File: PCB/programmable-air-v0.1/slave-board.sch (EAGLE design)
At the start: 18 parts, among them Q1 600mA/40V, Q2 600mA/40V, Q3 600mA/40V

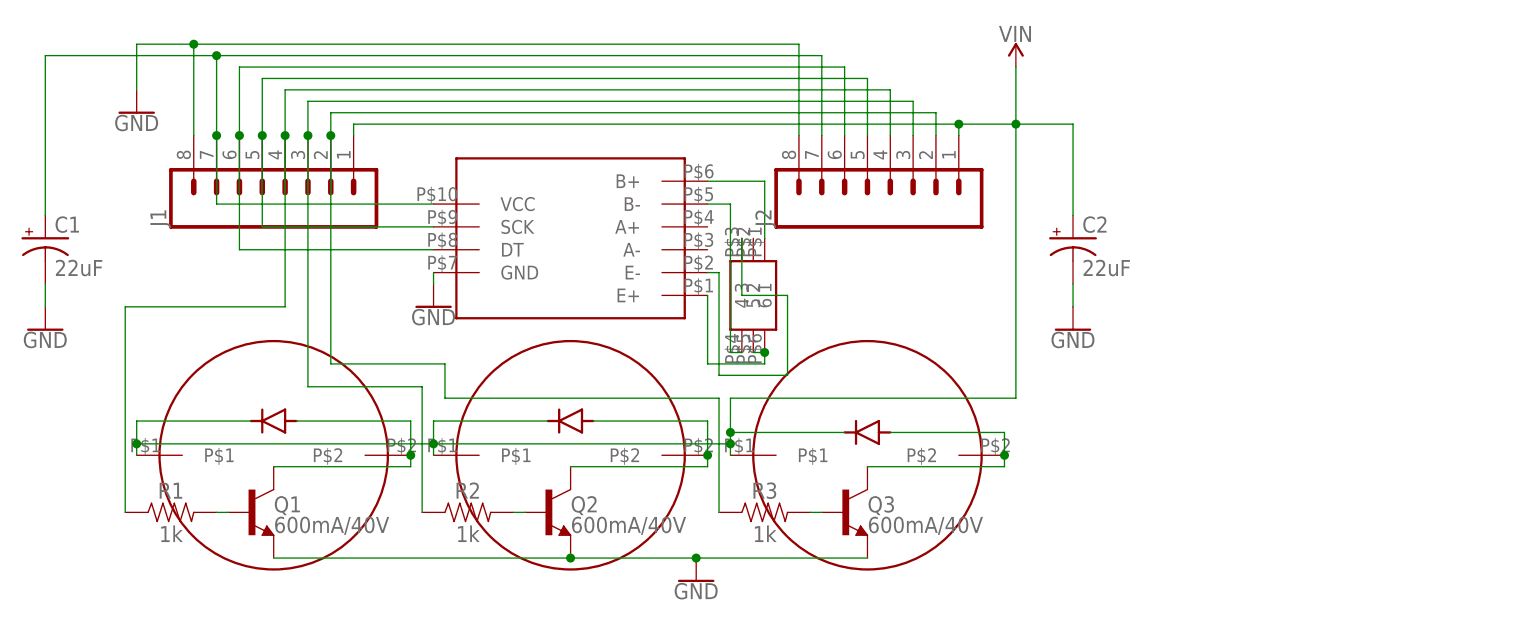
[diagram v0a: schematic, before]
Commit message: Modified slave board to have LM10CN
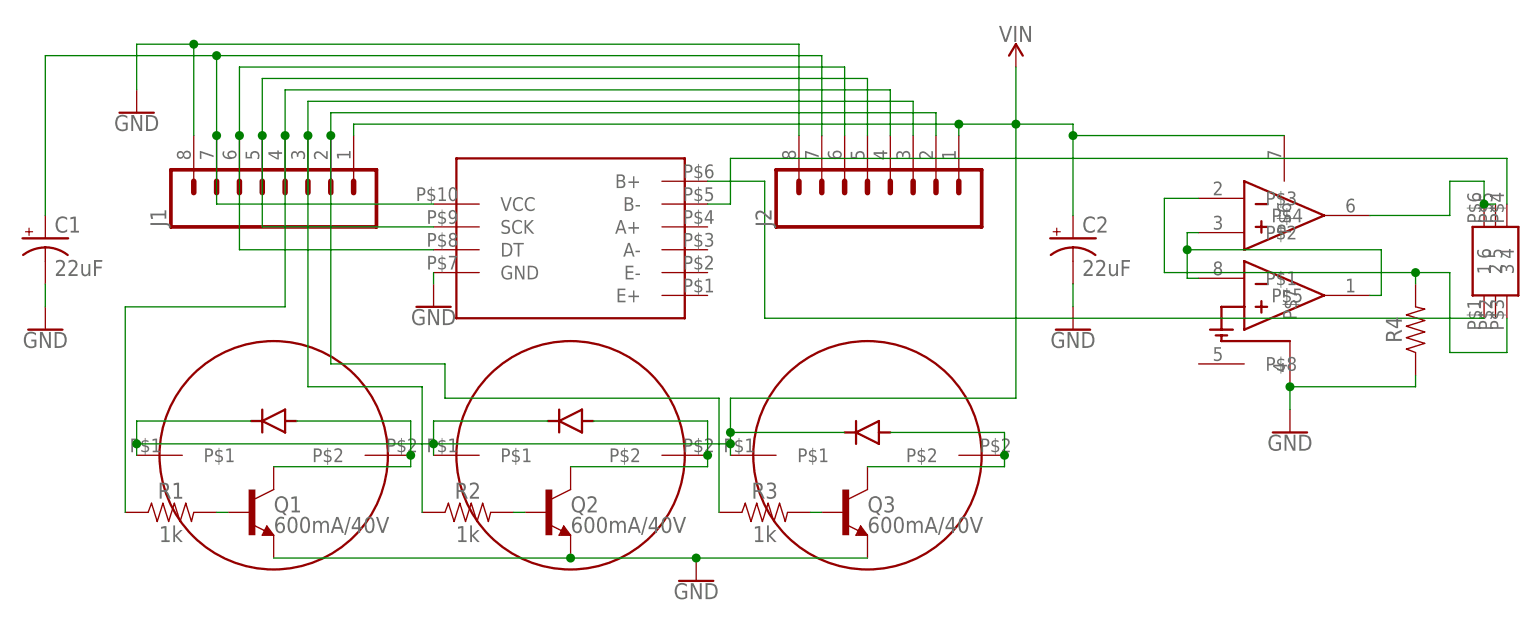
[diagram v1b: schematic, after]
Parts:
- added R4: (no value), SparkFun-Resistors:RESISTORAXIAL-0.3
- added U$9: LM10CN, programmable-air-components:LM10CN
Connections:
- removed net N$11: U$1.E+, U$8.5, U$8.6
- new net N$16: U$8.5, U$8.6, U$9.P$4
- new net N$4: U$9.P$1, U$9.P$2, U$9.P$5
- net GND: now also R4.1, U$9.P$7
- net N$17: now also R4.2, U$9.P$3; no longer U$1.E-
- net VIN: now also U$9.P$6
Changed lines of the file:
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@@
 <layers>
 <layer number="1" name="Top" color="4" fill="1" visible="no" active="no"/>
+<layer number="2" name="Route2" color="1" fill="3" visible="no" active="no"/>
+<layer number="3" name="Route3" color="4" fill="3" visible="no" active="no"/>
+<layer number="4" name="Route4" color="1" fill="4" visible="no" active="no"/>
+<layer number="5" name="Route5" color="4" fill="4" visible="no" active="no"/>
+<layer number="6" name="Route6" color="1" fill="8" visible="no" active="no"/>
+<layer number="7" name="Route7" color="4" fill="8" visible="no" active="no"/>
+<layer number="8" name="Route8" color="1" fill="2" visible="no" active="no"/>
+<layer number="9" name="Route9" color="4" fill="2" visible="no" active="no"/>
+<layer number="10" name="Route10" color="1" fill="7" visible="no" active="no"/>
+<layer number="11" name="Route11" color="4" fill="7" visible="no" active="no"/>
+<layer number="12" name="Route12" color="1" fill="5" visible="no" active="no"/>
+<layer number="13" name="Route13" color="4" fill="5" visible="no" active="no"/>
+<layer number="14" name="Route14" color="1" fill="6" visible="no" active="no"/>
+<layer number="15" name="Route15" color="4" fill="6" visible="no" active="no"/>
 <layer number="16" name="Bottom" color="1" fill="1" visible="no" active="no"/>
 <layer number="17" name="Pads" color="2" fill="1" visible="no" active="no"/>
@@
 <part name="GND4" library="SparkFun-PowerSymbols" deviceset="GND" device=""/>
 <part name="GND5" library="SparkFun-PowerSymbols" deviceset="GND" device=""/>
+<part name="U$9" library="programmable-air-components" deviceset="LM10CN" device=""/>
+<part name="R4" library="SparkFun-Resistors" deviceset="RESISTOR" device="AXIAL-0.3" value=" "/>
+<part name="GND6" library="SparkFun-PowerSymbols" deviceset="GND" device=""/>
 </parts>
 <sheets>
@@
 <instance part="GND2" gate="1" x="-48.26" y="27.94"/>
 <instance part="GND3" gate="1" x="-15.24" y="6.35"/>
-<instance part="U$8" gate="G$1" x="20.32" y="7.62" rot="R270"/>
+<instance part="U$8" gate="G$1" x="102.87" y="11.43" rot="R90"/>
 <instance part="C1" gate="G$1" x="-58.42" y="13.97"/>
 <instance part="C2" gate="G$1" x="55.88" y="13.97"/>
 <instance part="GND4" gate="1" x="-58.42" y="3.81"/>
 <instance part="GND5" gate="1" x="55.88" y="3.81"/>
+<instance part="U$9" gate="G$1" x="78.74" y="7.62"/>
+<instance part="R4" gate="G$1" x="93.98" y="3.81" rot="R90"/>
+<instance part="GND6" gate="1" x="80.01" y="-7.62"/>
 </instances>
 <busses>
@@
 <junction x="17.78" y="-8.89"/>
 <pinref part="C2" gate="G$1" pin="+"/>
-<wire x1="55.88" y1="16.51" x2="55.88" y2="26.67" width="0.1524" layer="91"/>
+<wire x1="55.88" y1="16.51" x2="55.88" y2="25.4" width="0.1524" layer="91"/>
+<wire x1="55.88" y1="25.4" x2="55.88" y2="26.67" width="0.1524" layer="91"/>
 <wire x1="49.53" y1="26.67" x2="55.88" y2="26.67" width="0.1524" layer="91"/>
+<pinref part="U$9" gate="G$1" pin="P$6"/>
+<wire x1="79.375" y1="25.4" x2="55.88" y2="25.4" width="0.1524" layer="91"/>
+<junction x="55.88" y="25.4"/>
 </segment>
 </net>
@@
 <wire x1="-58.42" y1="8.89" x2="-58.42" y2="6.35" width="0.1524" layer="91"/>
 </segment>
+<segment>
+<pinref part="U$9" gate="G$1" pin="P$7"/>
+<wire x1="80.01" y1="-2.54" x2="80.01" y2="-5.08" width="0.1524" layer="91"/>
+<pinref part="R4" gate="G$1" pin="1"/>
+<wire x1="93.98" y1="-1.27" x2="93.98" y2="-2.54" width="0.1524" layer="91"/>
+<wire x1="93.98" y1="-2.54" x2="80.01" y2="-2.54" width="0.1524" layer="91"/>
+<junction x="80.01" y="-2.54"/>
+<pinref part="GND6" gate="1" pin="GND"/>
+</segment>
+</net>
+<net name="N$16" class="0">
+<segment>
+<pinref part="U$8" gate="G$1" pin="6"/>
+<pinref part="U$8" gate="G$1" pin="5"/>
+<wire x1="102.87" y1="17.78" x2="101.6" y2="17.78" width="0.1524" layer="91"/>
+<pinref part="U$9" gate="G$1" pin="P$4"/>
+<wire x1="88.9" y1="16.51" x2="97.79" y2="16.51" width="0.1524" layer="91"/>
+<wire x1="97.79" y1="16.51" x2="97.79" y2="20.32" width="0.1524" layer="91"/>
+<wire x1="97.79" y1="20.32" x2="101.6" y2="20.32" width="0.1524" layer="91"/>
+<wire x1="101.6" y1="20.32" x2="101.6" y2="17.78" width="0.1524" layer="91"/>
+<junction x="101.6" y="17.78"/>
+</segment>
 </net>
 <net name="N$4" class="0">
 <segment>
+<pinref part="U$9" gate="G$1" pin="P$1"/>
+<wire x1="69.85" y1="9.525" x2="68.58" y2="9.525" width="0.1524" layer="91"/>
+<wire x1="68.58" y1="9.525" x2="68.58" y2="12.7" width="0.1524" layer="91"/>
+<wire x1="68.58" y1="12.7" x2="90.17" y2="12.7" width="0.1524" layer="91"/>
+<pinref part="U$9" gate="G$1" pin="P$5"/>
+<wire x1="88.9" y1="7.62" x2="90.17" y2="7.62" width="0.1524" layer="91"/>
+<wire x1="90.17" y1="7.62" x2="90.17" y2="12.7" width="0.1524" layer="91"/>
+<pinref part="U$9" gate="G$1" pin="P$2"/>
+<wire x1="69.85" y1="14.605" x2="68.58" y2="14.605" width="0.1524" layer="91"/>
+<wire x1="68.58" y1="14.605" x2="68.58" y2="12.7" width="0.1524" layer="91"/>
+<junction x="68.58" y="12.7"/>
+</segment>
+</net>
+<net name="N$17" class="0">
+<segment>
+<pinref part="U$9" gate="G$1" pin="P$3"/>
+<wire x1="69.85" y1="18.415" x2="66.04" y2="18.415" width="0.1524" layer="91"/>
+<wire x1="66.04" y1="18.415" x2="66.04" y2="10.16" width="0.1524" layer="91"/>
+<pinref part="R4" gate="G$1" pin="2"/>
+<wire x1="66.04" y1="10.16" x2="93.98" y2="10.16" width="0.1524" layer="91"/>
+<wire x1="93.98" y1="10.16" x2="93.98" y2="8.89" width="0.1524" layer="91"/>
+<pinref part="U$8" gate="G$1" pin="3"/>
+<wire x1="104.14" y1="5.08" x2="104.14" y2="1.27" width="0.1524" layer="91"/>
+<wire x1="104.14" y1="1.27" x2="97.79" y2="1.27" width="0.1524" layer="91"/>
+<wire x1="97.79" y1="1.27" x2="97.79" y2="10.16" width="0.1524" layer="91"/>
+<wire x1="97.79" y1="10.16" x2="93.98" y2="10.16" width="0.1524" layer="91"/>
+<junction x="93.98" y="10.16"/>
+</segment>
+</net>
+<net name="N$21" class="0">
+<segment>
 <pinref part="U$8" gate="G$1" pin="1"/>
+<wire x1="101.6" y1="5.08" x2="21.59" y2="5.08" width="0.1524" layer="91"/>
+<wire x1="21.59" y1="5.08" x2="21.59" y2="20.32" width="0.1524" layer="91"/>
 <pinref part="U$1" gate="G$1" pin="B+"/>
-<wire x1="21.59" y1="13.97" x2="21.59" y2="20.32" width="0.1524" layer="91"/>
 <wire x1="21.59" y1="20.32" x2="15.24" y2="20.32" width="0.1524" layer="91"/>
 </segment>
 </net>
-<net name="N$6" class="0">
-<segment>
+<net name="N$22" class="0">
+<segment>
+<pinref part="U$8" gate="G$1" pin="4"/>
+<wire x1="104.14" y1="17.78" x2="104.14" y2="22.86" width="0.1524" layer="91"/>
+<wire x1="104.14" y1="22.86" x2="17.78" y2="22.86" width="0.1524" layer="91"/>
+<wire x1="17.78" y1="22.86" x2="17.78" y2="17.78" width="0.1524" layer="91"/>
 <pinref part="U$1" gate="G$1" pin="B-"/>
-<wire x1="15.24" y1="17.78" x2="17.78" y2="17.78" width="0.1524" layer="91"/>
-<wire x1="17.78" y1="17.78" x2="17.78" y2="1.27" width="0.1524" layer="91"/>
-<pinref part="U$8" gate="G$1" pin="4"/>
-<wire x1="17.78" y1="1.27" x2="19.05" y2="1.27" width="0.1524" layer="91"/>
-</segment>
-</net>
-<net name="N$11" class="0">
-<segment>
-<wire x1="15.24" y1="0" x2="21.59" y2="0" width="0.1524" layer="91"/>
-<pinref part="U$8" gate="G$1" pin="6"/>
-<wire x1="21.59" y1="0" x2="21.59" y2="1.27" width="0.1524" layer="91"/>
-<pinref part="U$8" gate="G$1" pin="5"/>
-<wire x1="20.32" y1="1.27" x2="21.59" y2="1.27" width="0.1524" layer="91"/>
-<junction x="21.59" y="1.27"/>
-<pinref part="U$1" gate="G$1" pin="E+"/>
-<wire x1="15.24" y1="0" x2="15.24" y2="7.62" width="0.1524" layer="91"/>
-</segment>
-</net>
-<net name="N$17" class="0">
-<segment>
-<pinref part="U$1" gate="G$1" pin="E-"/>
-<wire x1="15.24" y1="10.16" x2="16.51" y2="10.16" width="0.1524" layer="91"/>
-<pinref part="U$8" gate="G$1" pin="3"/>
-<wire x1="19.05" y1="13.97" x2="19.05" y2="7.62" width="0.1524" layer="91"/>
-<wire x1="19.05" y1="7.62" x2="24.13" y2="7.62" width="0.1524" layer="91"/>
-<wire x1="24.13" y1="7.62" x2="24.13" y2="-1.27" width="0.1524" layer="91"/>
-<wire x1="24.13" y1="-1.27" x2="16.51" y2="-1.27" width="0.1524" layer="91"/>
-<wire x1="16.51" y1="10.16" x2="16.51" y2="-1.27" width="0.1524" layer="91"/>
-</segment>
-</net>
+<wire x1="17.78" y1="17.78" x2="15.24" y2="17.78" width="0.1524" layer="91"/>
+</segment>
+</net>

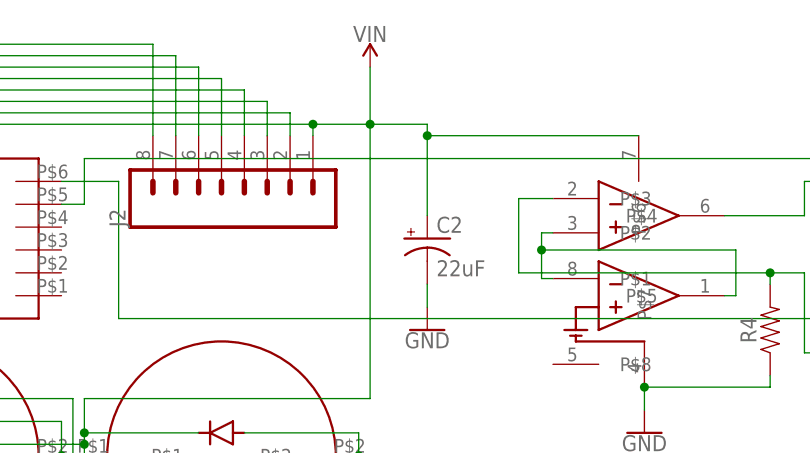
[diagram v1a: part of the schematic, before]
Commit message: Added PCB for testing SMPP with LM10 and HX711. Added gitignore.
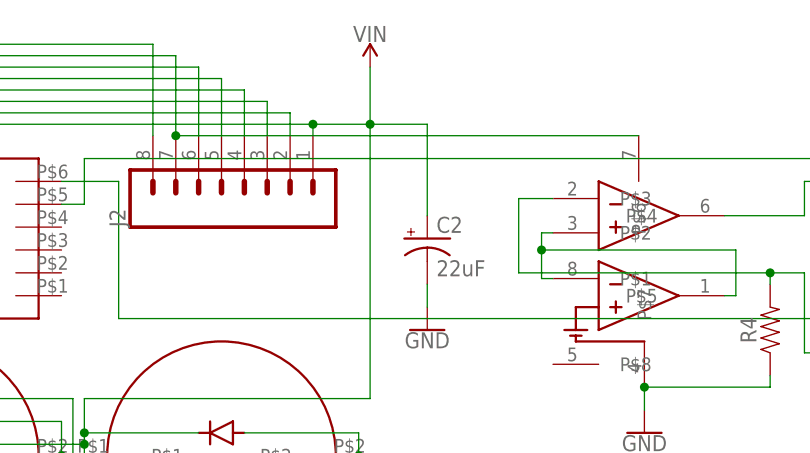
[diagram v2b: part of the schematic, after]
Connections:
- net N$15: now also U$9.P$6
- net VIN: no longer U$9.P$6
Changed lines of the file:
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@@
 <setting verticaltext="up"/>
 </settings>
-<grid distance="0.05" unitdist="inch" unit="inch" style="lines" multiple="1" display="no" altdistance="0.01" altunitdist="inch" altunit="inch"/>
+<grid distance="0.1" unitdist="inch" unit="inch" style="lines" multiple="1" display="no" altdistance="0.01" altunitdist="inch" altunit="inch"/>
 <layers>
 <layer number="1" name="Top" color="4" fill="1" visible="no" active="no"/>
@@
 <junction x="-39.37" y="34.29"/>
 <junction x="-39.37" y="25.4"/>
+<pinref part="U$9" gate="G$1" pin="P$6"/>
+<wire x1="27.94" y1="25.4" x2="79.375" y2="25.4" width="0.1524" layer="91"/>
+<junction x="27.94" y="25.4"/>
 </segment>
 </net>
@@
 <junction x="17.78" y="-8.89"/>
 <pinref part="C2" gate="G$1" pin="+"/>
-<wire x1="55.88" y1="16.51" x2="55.88" y2="25.4" width="0.1524" layer="91"/>
-<wire x1="55.88" y1="25.4" x2="55.88" y2="26.67" width="0.1524" layer="91"/>
+<wire x1="55.88" y1="16.51" x2="55.88" y2="26.67" width="0.1524" layer="91"/>
 <wire x1="49.53" y1="26.67" x2="55.88" y2="26.67" width="0.1524" layer="91"/>
-<pinref part="U$9" gate="G$1" pin="P$6"/>
-<wire x1="79.375" y1="25.4" x2="55.88" y2="25.4" width="0.1524" layer="91"/>
-<junction x="55.88" y="25.4"/>
-</segment>
-</net>
+</segment>
+</net>
